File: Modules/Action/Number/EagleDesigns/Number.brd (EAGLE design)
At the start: 100 x 80 mm, 9 parts, among them U2 ATMEGA328P_TQFP

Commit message: fixed eagle files for new modules
SIN/SOUT was not correctly connected in them.
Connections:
- removed net 1X3SIN: U2.23
- net 1X3SIN-SOUT: now also U2.23
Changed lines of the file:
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@@
 <wire x1="18.5" y1="3.9" x2="17.6" y2="2.6" width="0.3048" layer="16"/>
 <wire x1="17.6" y1="2.6" x2="16.04" y2="2.66" width="0.3048" layer="16"/>
+<contactref element="U2" pad="23"/>
+<wire x1="8.7" y1="4.5" x2="5.8074" y2="14.54" width="0" layer="19" extent="1-16"/>
 </signal>
 <signal name="RESET">
@@
 <wire x1="14.8" y1="20.15" x2="14.76" y2="20.39" width="0.3048" layer="16"/>
 </signal>
-<signal name="1X3SIN">
-<contactref element="U2" pad="23"/>
-</signal>
 <signal name="N$1">

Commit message: Number: added final PCB #32
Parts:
- moved U2 0.71 mm to (10.0, 13.2)
- moved U$1 0.51 mm to (9.30, 5.40)
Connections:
- removed net SCL: U2.28
- removed net SDA: U2.27
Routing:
- net 1X3SIN-SOUT: track 15.4 -> 31.7 mm
- net 7SEG-G: track 16.1 -> 8.17 mm
- net GND: track 54.2 -> 46.2 mm, vias 1 -> 2
- net 7SEG-E: track 6.25 -> 3.67 mm
- net 7SEG-F: track 10.4 -> 8.41 mm
- net 7SEG-C: track 4.22 -> 5.80 mm
- net 7SEG-D: track 2.43 -> 3.71 mm
- net N$3: track 7.13 -> 8.37 mm
- net RX: track 3.94 -> 3.28 mm

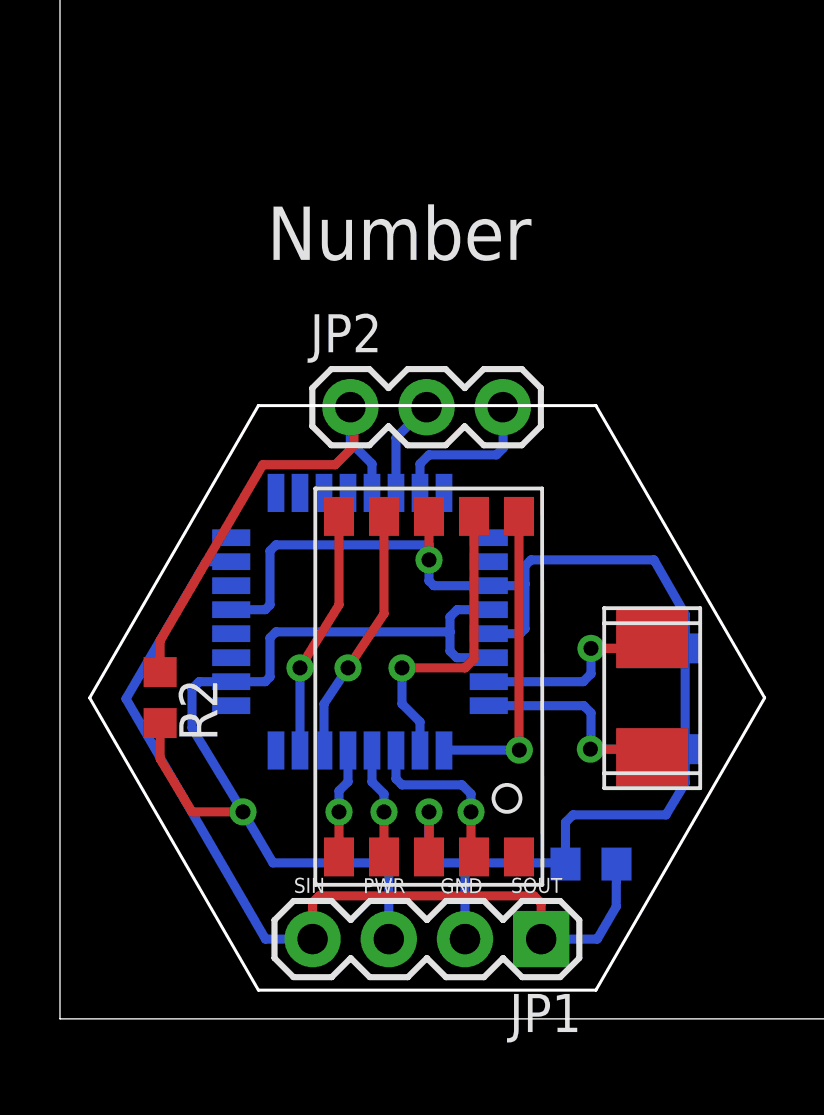
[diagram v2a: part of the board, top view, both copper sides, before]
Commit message: added version numbers, and deleted most of the text that was on each module.
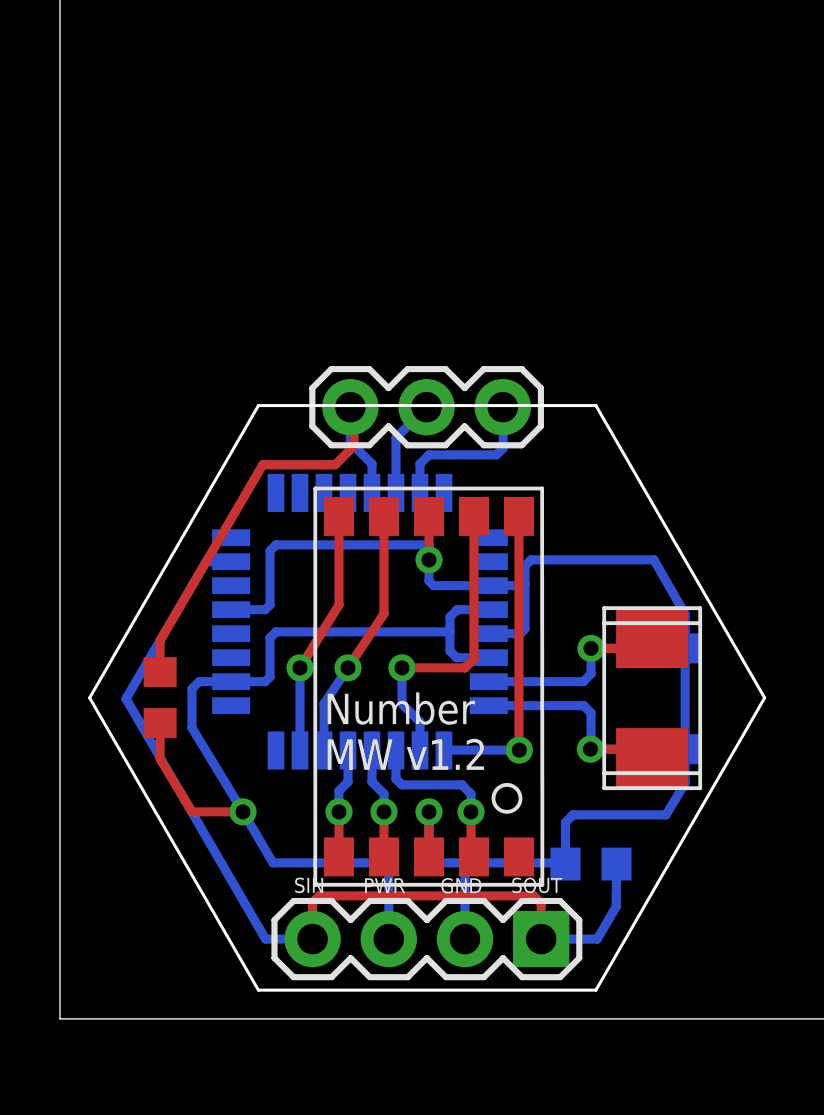
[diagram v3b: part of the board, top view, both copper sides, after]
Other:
- board text added: "Number MW v1.2"
- board text removed: "Number"
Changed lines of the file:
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@@
 <layer number="19" name="Unrouted" color="6" fill="1" visible="yes" active="yes"/>
 <layer number="20" name="Dimension" color="15" fill="1" visible="yes" active="yes"/>
-<layer number="21" name="tPlace" color="7" fill="1" visible="no" active="yes"/>
-<layer number="22" name="bPlace" color="7" fill="1" visible="no" active="yes"/>
+<layer number="21" name="tPlace" color="7" fill="1" visible="yes" active="yes"/>
+<layer number="22" name="bPlace" color="7" fill="1" visible="yes" active="yes"/>
 <layer number="23" name="tOrigins" color="15" fill="1" visible="yes" active="yes"/>
 <layer number="24" name="bOrigins" color="15" fill="1" visible="yes" active="yes"/>
-<layer number="25" name="tNames" color="7" fill="1" visible="no" active="yes"/>
-<layer number="26" name="bNames" color="7" fill="1" visible="no" active="yes"/>
-<layer number="27" name="tValues" color="7" fill="1" visible="no" active="yes"/>
-<layer number="28" name="bValues" color="7" fill="1" visible="no" active="yes"/>
+<layer number="25" name="tNames" color="7" fill="1" visible="yes" active="yes"/>
+<layer number="26" name="bNames" color="7" fill="1" visible="yes" active="yes"/>
+<layer number="27" name="tValues" color="7" fill="1" visible="yes" active="yes"/>
+<layer number="28" name="bValues" color="7" fill="1" visible="yes" active="yes"/>
 <layer number="29" name="tStop" color="7" fill="3" visible="no" active="yes"/>
 <layer number="30" name="bStop" color="7" fill="6" visible="no" active="yes"/>
@@
 <text x="12.6723" y="4.188" size="0.5" layer="21">GND</text>
 <text x="15.0345" y="4.2007" size="0.5" layer="21">SOUT</text>
-<text x="6.9" y="25.3" size="1.778" layer="21">Number</text>
+<text x="8.8" y="8.3" size="1.016" layer="21">Number
+MW v1.2</text>
 </plain>
 <attributes>
@@
 </autorouter>
 <elements>
-<element name="C1" library="adafruit" package="C0603" value="22pF" x="20" y="12.35" rot="MR180"/>
-<element name="C2" library="adafruit" package="C0603" value="22pF" x="19.99" y="8.99" rot="MR180"/>
-<element name="JP1" library="SparkFun-Connectors" package="1X04" value="" x="16.04" y="2.66" rot="R180"/>
-<element name="JP2" library="SparkFun-Connectors" package="1X03" value="" x="9.68" y="20.39"/>
-<element name="R1" library="adafruit" package="R0603" value="1M" x="17.7" y="5.16" rot="MR180"/>
-<element name="R2" library="resistor" package="R0603" value="10K" x="3.34" y="10.71" rot="R270"/>
-<element name="U$2" library="MakerWear" package="NX503" value="NX503" x="19.74" y="10.69" rot="R270"/>
-<element name="U2" library="SparkFun-DigitalIC" package="TQFP32-08" value="ATMEGA328P_TQFP" x="10" y="13.24" rot="MR0">
+<element name="C1" library="adafruit" package="C0603" value="22pF" x="20" y="12.35" smashed="yes" rot="MR180"/>
+<element name="C2" library="adafruit" package="C0603" value="22pF" x="19.99" y="8.99" smashed="yes" rot="MR180"/>
+<element name="JP1" library="SparkFun-Connectors" package="1X04" value="" x="16.04" y="2.66" smashed="yes" rot="R180">
+<attribute name="VALUE" x="17.31" y="5.835" size="1.27" layer="27" rot="R180"/>
+</element>
+<element name="JP2" library="SparkFun-Connectors" package="1X03" value="" x="9.68" y="20.39" smashed="yes">
+<attribute name="VALUE" x="8.41" y="17.215" size="1.27" layer="27"/>
+</element>
+<element name="R1" library="adafruit" package="R0603" value="1M" x="17.7" y="5.16" smashed="yes" rot="MR180"/>
+<element name="R2" library="resistor" package="R0603" value="10K" x="3.34" y="10.71" smashed="yes" rot="R270"/>
+<element name="U$2" library="MakerWear" package="NX503" value="NX503" x="19.74" y="10.69" smashed="yes" rot="R270"/>
+<element name="U2" library="SparkFun-DigitalIC" package="TQFP32-08" value="ATMEGA328P_TQFP" x="10" y="13.24" smashed="yes" rot="MR0">
 <attribute name="PROD_ID" value="IC-09069" x="10" y="13.24" size="1.778" layer="28" rot="MR0" display="off"/>
 </element>
-<element name="U$1" library="MakerWear" package="7SEG-SMD-10X7.3" value="7SEGMENT" x="9.3" y="5.4"/>
+<element name="U$1" library="MakerWear" package="7SEG-SMD-10X7.3" value="7SEGMENT" x="9.3" y="5.4" smashed="yes"/>
 </elements>
 <signals>
@@
 </board>
 </drawing>
+<compatibility>
+<note version="6.3" minversion="6.2.2" severity="warning">
+Since Version 6.2.2 text objects can contain more than one line,
+which will not be processed correctly with this version.
+</note>
+</compatibility>
 </eagle>

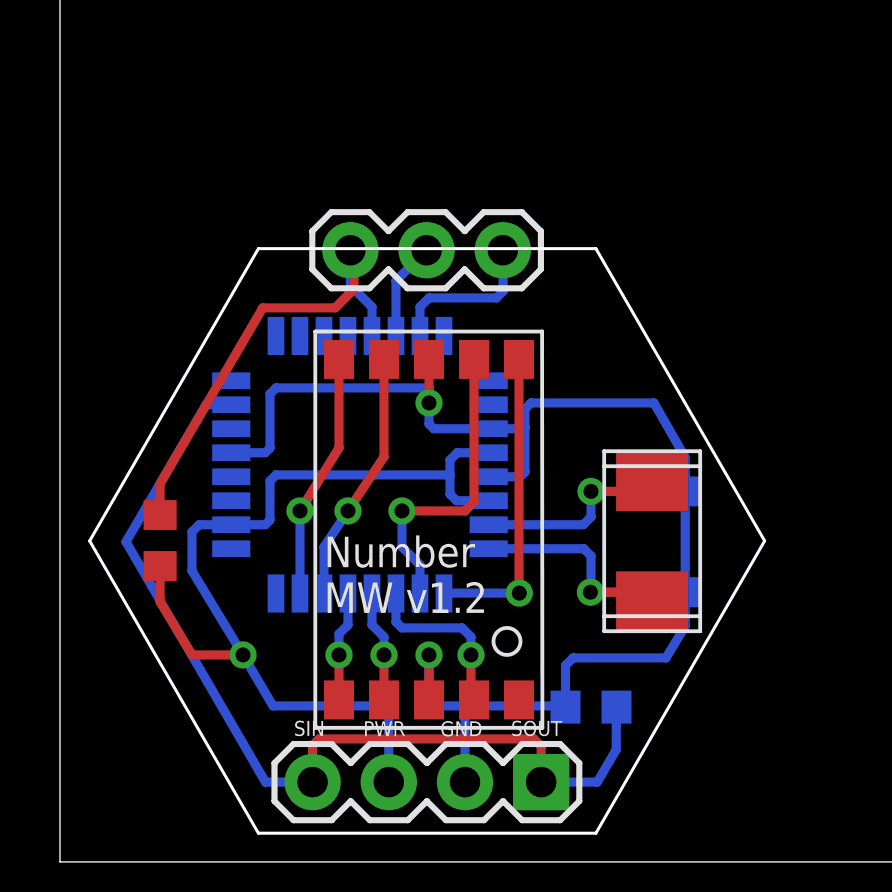
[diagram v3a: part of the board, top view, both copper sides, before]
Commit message: Removed crystal and added resistor on 7-seg
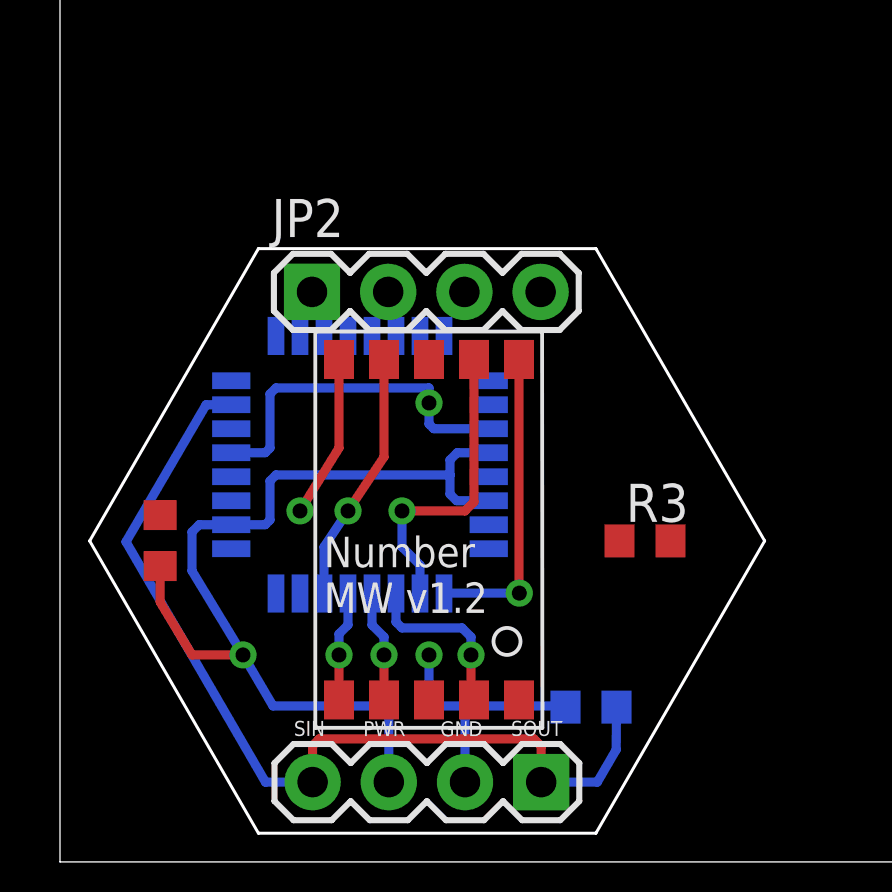
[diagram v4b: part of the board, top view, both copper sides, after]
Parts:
- removed C1, C2: 22pF, adafruit:C0603
- removed U$2: NX503, MakerWear:NX503
- added R3: 330, resistor:R0603
- JP2: device SparkFun-Connectors:1X03 -> SparkFun-Connectors:1X04
- moved JP2 1.89 mm to (8.40, 19.0)
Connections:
- removed net N$3: C2.1, U$2.P$2, U2.8
- new net 7SEG-G/MOSI: JP2.2, U2.15
- new net MISO: JP2.3, U2.16
- new net SCK: JP2.4, U2.17
- net 7SEG-G: no longer U2.15
- net GND: now also R3.1; no longer C1.2, C2.2, U$1.GND1, U$1.GND2
- net N$1: now also R3.2, U$1.GND2; no longer C1.1, U$2.P$1, U2.7
- net RX: no longer JP2.2
- net TX: no longer JP2.3
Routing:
- net GND: track 46.2 -> 20.5 mm
- net RESET: track 15.6 -> 0.00 mm
- net N$3: track 8.37 -> 0.00 mm, vias 1 -> 0
- net N$1: track 8.00 -> 0.00 mm, vias 1 -> 0
- net TX: track 5.33 -> 0.00 mm
- net RX: track 3.28 -> 0.00 mm
- net 7SEG-G: track 8.17 -> 5.42 mm
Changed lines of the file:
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@@
 <?xml version="1.0" encoding="utf-8"?>
 <!DOCTYPE eagle SYSTEM "eagle.dtd">
-<eagle version="7.3.0">
+<eagle version="7.6.0">
 <drawing>
 <settings>
@@
 </autorouter>
 <elements>
-<element name="C1" library="adafruit" package="C0603" value="22pF" x="20" y="12.35" smashed="yes" rot="MR180"/>
-<element name="C2" library="adafruit" package="C0603" value="22pF" x="19.99" y="8.99" smashed="yes" rot="MR180"/>
 <element name="JP1" library="SparkFun-Connectors" package="1X04" value="" x="16.04" y="2.66" smashed="yes" rot="R180">
 <attribute name="VALUE" x="17.31" y="5.835" size="1.27" layer="27" rot="R180"/>
 </element>
-<element name="JP2" library="SparkFun-Connectors" package="1X03" value="" x="9.68" y="20.39" smashed="yes">
-<attribute name="VALUE" x="8.41" y="17.215" size="1.27" layer="27"/>
-</element>
 <element name="R1" library="adafruit" package="R0603" value="1M" x="17.7" y="5.16" smashed="yes" rot="MR180"/>
 <element name="R2" library="resistor" package="R0603" value="10K" x="3.34" y="10.71" smashed="yes" rot="R270"/>
-<element name="U$2" library="MakerWear" package="NX503" value="NX503" x="19.74" y="10.69" smashed="yes" rot="R270"/>
 <element name="U2" library="SparkFun-DigitalIC" package="TQFP32-08" value="ATMEGA328P_TQFP" x="10" y="13.24" smashed="yes" rot="MR0">
 <attribute name="PROD_ID" value="IC-09069" x="10" y="13.24" size="1.778" layer="28" rot="MR0" display="off"/>
 </element>
 <element name="U$1" library="MakerWear" package="7SEG-SMD-10X7.3" value="7SEGMENT" x="9.3" y="5.4" smashed="yes"/>
+<element name="JP2" library="SparkFun-Connectors" package="1X04" value="" x="8.4" y="19"/>
+<element name="R3" library="resistor" package="R0603" value="330" x="19.5" y="10.7"/>
 </elements>
 <signals>
@@
 <contactref element="U2" pad="3"/>
 <contactref element="U2" pad="21"/>
-<contactref element="C1" pad="2"/>
-<contactref element="C2" pad="2"/>
-<contactref element="U$1" pad="GND2"/>
-<contactref element="U$1" pad="GND1"/>
-<wire x1="14.2926" y1="12.84" x2="15.34" y2="12.84" width="0.3048" layer="16"/>
-<wire x1="15.34" y1="12.84" x2="15.5" y2="13" width="0.3048" layer="16"/>
-<wire x1="15.5" y1="13" x2="15.5" y2="14.5" width="0.3048" layer="16"/>
-<wire x1="15.5" y1="14.5" x2="15.5" y2="15.1" width="0.3048" layer="16"/>
-<wire x1="15.5" y1="15.1" x2="15.7" y2="15.3" width="0.3048" layer="16"/>
-<wire x1="15.7" y1="15.3" x2="19.8" y2="15.3" width="0.3048" layer="16"/>
-<wire x1="19.8" y1="15.3" x2="20.84" y2="13.48" width="0.3048" layer="16"/>
-<wire x1="20.84" y1="13.48" x2="20.85" y2="12.35" width="0.3048" layer="16"/>
-<wire x1="14.2926" y1="14.44" x2="15.44" y2="14.44" width="0.3048" layer="16"/>
-<wire x1="15.44" y1="14.44" x2="15.5" y2="14.5" width="0.3048" layer="16"/>
-<wire x1="12.3" y1="5.4" x2="12.3" y2="6.9" width="0.3048" layer="1"/>
 <via x="12.3" y="6.9" extent="1-16" drill="0.5"/>
 <wire x1="12.3" y1="6.9" x2="12.3" y2="5.4" width="0.3048" layer="16"/>
@@
 <wire x1="16.81" y1="5.2" x2="16.85" y2="5.16" width="0.3048" layer="16"/>
 <wire x1="13.5" y1="2.66" x2="13.5" y2="5.2" width="0.3048" layer="16"/>
-<wire x1="16.85" y1="5.16" x2="16.85" y2="6.55" width="0.3048" layer="16"/>
-<wire x1="16.85" y1="6.55" x2="17.1" y2="6.8" width="0.3048" layer="16"/>
-<wire x1="17.1" y1="6.8" x2="20.2" y2="6.8" width="0.3048" layer="16"/>
-<wire x1="20.2" y1="6.8" x2="20.84" y2="7.86" width="0.3048" layer="16"/>
-<wire x1="20.84" y1="7.86" x2="20.84" y2="8.99" width="0.3048" layer="16"/>
-<wire x1="20.84" y1="8.99" x2="20.84" y2="12.34" width="0.3048" layer="16"/>
-<wire x1="20.84" y1="12.34" x2="20.85" y2="12.35" width="0.3048" layer="16"/>
 <wire x1="5.7074" y1="13.64" x2="6.84" y2="13.64" width="0.3048" layer="16"/>
 <wire x1="6.84" y1="13.64" x2="7" y2="13.8" width="0.3048" layer="16"/>
@@
 <wire x1="7" y1="15.6" x2="7.2" y2="15.8" width="0.3048" layer="16"/>
 <wire x1="14.2826" y1="14.43" x2="14.2926" y2="14.44" width="0.3048" layer="16"/>
-<wire x1="12.3" y1="16.75" x2="12.3" y2="15.3" width="0.3048" layer="1"/>
 <via x="12.3" y="15.3" extent="1-16" drill="0.5"/>
 <wire x1="12.3" y1="15.3" x2="12.3" y2="15.8" width="0.3048" layer="16"/>
@@
 <wire x1="12.46" y1="14.44" x2="12.3" y2="14.6" width="0.3048" layer="16"/>
 <wire x1="12.3" y1="14.6" x2="12.3" y2="15.3" width="0.3048" layer="16"/>
+<contactref element="R3" pad="1"/>
+<wire x1="14.2926" y1="14.44" x2="14.2926" y2="12.84" width="0" layer="19" extent="16-16"/>
+<wire x1="12.3" y1="6.9" x2="14.2926" y2="12.84" width="0" layer="19" extent="16-16"/>
+<wire x1="18.65" y1="10.7" x2="13.5" y2="2.66" width="0" layer="19" extent="1-1"/>
 </signal>
 <signal name="1X3SIN-SOUT">
@@
 </signal>
 <signal name="RESET">
-<contactref element="JP2" pad="1"/>
 <contactref element="U2" pad="29"/>
 <contactref element="R2" pad="1"/>
-<wire x1="9.68" y1="20.39" x2="9.68" y2="19.22" width="0.3048" layer="16"/>
-<wire x1="9.68" y1="19.22" x2="10.4" y2="18.5" width="0.3048" layer="16"/>
-<wire x1="10.4" y1="18.5" x2="10.4" y2="17.5326" width="0.3048" layer="16"/>
-<wire x1="3.34" y1="11.56" x2="3.34" y2="12.61" width="0.3048" layer="1"/>
-<wire x1="3.34" y1="12.61" x2="6.76" y2="18.47" width="0.3048" layer="1"/>
-<wire x1="6.76" y1="18.47" x2="9.17" y2="18.47" width="0.3048" layer="1"/>
-<wire x1="9.17" y1="18.47" x2="9.8" y2="19.1" width="0.3048" layer="1"/>
-<wire x1="9.8" y1="19.1" x2="9.8" y2="20.27" width="0.3048" layer="1"/>
-<wire x1="9.8" y1="20.27" x2="9.68" y2="20.39" width="0.3048" layer="1"/>
+<contactref element="JP2" pad="1"/>
+<wire x1="3.34" y1="11.56" x2="10.4" y2="17.5326" width="0" layer="19" extent="1-16"/>
+<wire x1="8.4" y1="19" x2="3.34" y2="11.56" width="0" layer="19" extent="1-1"/>
 </signal>
 <signal name="RX">
-<contactref element="JP2" pad="2"/>
 <contactref element="U2" pad="30"/>
-<wire x1="11.2" y1="17.5326" x2="11.2" y2="19.37" width="0.3048" layer="16"/>
-<wire x1="11.2" y1="19.37" x2="12.22" y2="20.39" width="0.3048" layer="16"/>
 </signal>
 <signal name="TX">
-<contactref element="JP2" pad="3"/>
 <contactref element="U2" pad="31"/>
-<wire x1="12" y1="17.5326" x2="12" y2="18.5" width="0.3048" layer="16"/>
-<wire x1="12" y1="18.5" x2="12.3" y2="18.8" width="0.3048" layer="16"/>
-<wire x1="12.3" y1="18.8" x2="14.55" y2="18.8" width="0.3048" layer="16"/>
-<wire x1="14.55" y1="18.8" x2="14.77" y2="19.02" width="0.3048" layer="16"/>
-<wire x1="14.77" y1="19.02" x2="14.77" y2="20.38" width="0.3048" layer="16"/>
-<wire x1="14.77" y1="20.38" x2="14.76" y2="20.39" width="0.3048" layer="16"/>
-</signal>
-<signal name="N$1">
-<contactref element="U$2" pad="P$1"/>
-<contactref element="U2" pad="7"/>
-<contactref element="C1" pad="1"/>
-<wire x1="19.15" y1="12.35" x2="17.7" y2="12.35" width="0.3048" layer="16"/>
-<via x="17.7" y="12.35" extent="1-16" drill="0.5"/>
-<wire x1="17.7" y1="12.35" x2="19.4" y2="12.35" width="0.3048" layer="1"/>
-<wire x1="19.4" y1="12.35" x2="19.74" y2="12.69" width="0.3048" layer="1"/>
-<wire x1="14.2926" y1="11.24" x2="17.44" y2="11.24" width="0.3048" layer="16"/>
-<wire x1="17.44" y1="11.24" x2="17.7" y2="11.5" width="0.3048" layer="16"/>
-<wire x1="17.7" y1="11.5" x2="17.7" y2="12.35" width="0.3048" layer="16"/>
-</signal>
-<signal name="N$3">
-<contactref element="U$2" pad="P$2"/>
-<contactref element="U2" pad="8"/>
-<contactref element="C2" pad="1"/>
-<wire x1="19.14" y1="8.99" x2="17.68" y2="8.99" width="0.3048" layer="16"/>
-<via x="17.68" y="8.99" extent="1-16" drill="0.5"/>
-<wire x1="17.68" y1="8.99" x2="19.44" y2="8.99" width="0.3048" layer="1"/>
-<wire x1="19.44" y1="8.99" x2="19.74" y2="8.69" width="0.3048" layer="1"/>
-<wire x1="14.2926" y1="10.44" x2="17.46" y2="10.44" width="0.3048" layer="16"/>
-<wire x1="17.46" y1="10.44" x2="17.7" y2="10.2" width="0.3048" layer="16"/>
-<wire x1="17.7" y1="10.2" x2="17.7" y2="9.01" width="0.3048" layer="16"/>
-<wire x1="17.7" y1="9.01" x2="17.68" y2="8.99" width="0.3048" layer="16"/>
 </signal>
 <signal name="7SEG-A">
@@
 </signal>
 <signal name="7SEG-G">
-<contactref element="U2" pad="15"/>
 <contactref element="U$1" pad="G"/>
 <wire x1="9.3" y1="16.75" x2="9.3" y2="13.8" width="0.3048" layer="1"/>
 <wire x1="9.3" y1="13.8" x2="8" y2="11.7" width="0.3048" layer="1"/>
 <via x="8" y="11.7" extent="1-16" drill="0.5"/>
-<wire x1="8" y1="11.7" x2="8" y2="8.9474" width="0.3048" layer="16"/>
+</signal>
+<signal name="N$1">
+<contactref element="U$1" pad="GND2"/>
+<contactref element="R3" pad="2"/>
+<wire x1="20.35" y1="10.7" x2="12.3" y2="16.75" width="0" layer="19" extent="1-1"/>
+</signal>
+<signal name="SCK">
+<contactref element="JP2" pad="4"/>
+<contactref element="U2" pad="17"/>
+<wire x1="16.02" y1="19" x2="5.7074" y2="10.44" width="0" layer="19" extent="16-16"/>
+</signal>
+<signal name="MISO">
+<contactref element="JP2" pad="3"/>
+<contactref element="U2" pad="16"/>
+<wire x1="13.48" y1="19" x2="7.2" y2="8.9474" width="0" layer="19" extent="16-16"/>
+</signal>
+<signal name="7SEG-G/MOSI">
+<contactref element="U2" pad="15"/>
+<contactref element="JP2" pad="2"/>
+<wire x1="10.94" y1="19" x2="8" y2="8.9474" width="0" layer="19" extent="16-16"/>
 </signal>
 </signals>
